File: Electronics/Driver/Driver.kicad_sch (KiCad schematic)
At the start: 14 parts, among them U1 DRV8428RTER, U2 DB125-2.54-4P-GN, U3 DB125-2.54-4P-GN

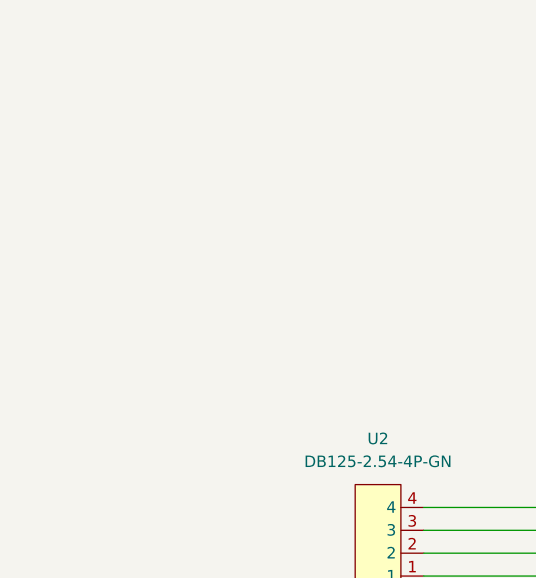
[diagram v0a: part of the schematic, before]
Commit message: Added driver PCB
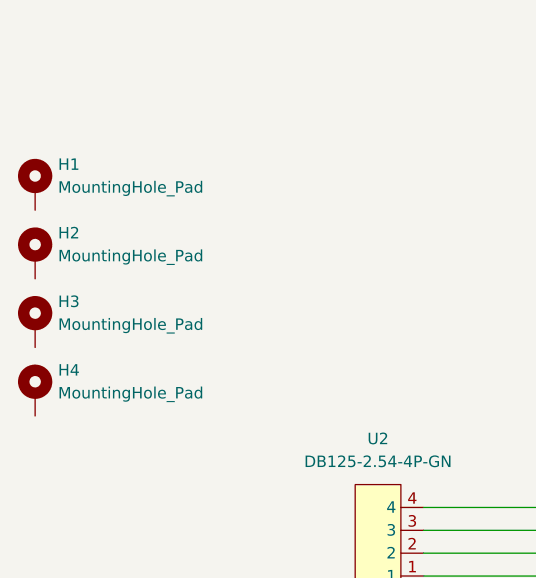
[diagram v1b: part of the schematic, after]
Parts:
- added H1, H2, H3, H4: MountingHole_Pad, MountingHole:MountingHole_3.2mm_M3_DIN965_Pad_TopBottom, symbol Mechanical:MountingHole_Pad

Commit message: Updated driver PCB
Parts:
- removed DC1, DC2: DC-005-20A_C136744, COMPONENTS:DC-IN-TH_DC-005-20A, symbol COMPONENTS:DC-005-20A_C136744
- removed H1, H2, H3, H4: MountingHole_Pad, MountingHole:MountingHole_3.2mm_M3_DIN965_Pad_TopBottom, symbol Mechanical:MountingHole_Pad
- removed R1, R2, R3, R4, R5, R6: 0, Resistor_SMD:R_1206_3216Metric_Pad1.30x1.75mm_HandSolder, symbol Device:R
- removed U2, U3: DB125-2.54-4P-GN, COMPONENTS:CONN-TH_DB125-2.54-4P-GN, symbol COMPONENTS:DB125-2.54-4P-GN
- added C4, C5, C6, C7: 0.1u, Capacitor_SMD:C_1206_3216Metric_Pad1.33x1.80mm_HandSolder, symbol Device:C
- added J1, J2: Conn_01x10_Pin, Connector_PinSocket_2.54mm:PinSocket_1x10_P2.54mm_Vertical, symbol Connector:Conn_01x10_Pin
- added U4, U5: SN74LVC1G125DBVR, COMPONENTS:SOT-23-5_L3.0-W1.7-P0.95-LS2.8-BL, symbol COMPONENTS:SN74LVC1G125DBVR
- added U6: MCP4725A0T-E/CH, COMPONENTS:SOT-23-6_L2.9-W1.6-P0.95-LS2.8-BL, symbol COMPONENTS:MCP4725A0T-E_CH
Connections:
- net +24V: now also J1.1 (Pin_1)
- net +3.3V: now also C4.2, C5.2, C7.2, J2.1 (Pin_1), U4.5 (VCC), U5.5 (VCC), U6.3 (VDD); no longer C3.2, U1.6 (DVDD)
- net GND: now also C4.1, C5.1, C6.1, C7.1, J1.10 (Pin_10), J1.2 (Pin_2), J1.9 (Pin_9), J2.10 (Pin_10), U4.3 (GND), U5.3 (GND), U6.2 (VSS), U6.6 (A0)
- net at U1.1 (AOUT1): now also J1.3 (Pin_3)
- net at U1.10 (M1): now also U4.4 (Y)
- net at U1.11 (STEP): now also J2.5 (Pin_5)
- net at U1.12 (DIR): now also J2.4 (Pin_4)
- net at U1.13 (EN/nFAULT): now also J2.3 (Pin_3)
- net at U1.14 (nSLEEP): now also J2.2 (Pin_2)
- net at U1.2 (AOUT2): now also J1.4 (Pin_4)
- net at U1.3 (BOUT2): now also J1.5 (Pin_5)
- net at U1.4 (BOUT1): now also J1.6 (Pin_6)
- net at U1.7 (VREF): now also C6.2, U6.1 (VOUT)
- net at U1.8 (M0): now also U5.4 (Y)
- new net: C3.2, U1.6 (DVDD)
- new net  s/3: J2.9 (Pin_9), U5.1 (OE)
- new net SCL: J1.8 (Pin_8), U6.5 (SCL)
- new net SDA: J1.7 (Pin_7), U6.4 (SDA)
- new net s/0: J2.6 (Pin_6), U4.2 (A)
- new net s/1: J2.7 (Pin_7), U4.1 (OE)
- new net s/2: J2.8 (Pin_8), U5.2 (A)
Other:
- note added: "Microstep Truth Table"
- moved on the sheet: C3
